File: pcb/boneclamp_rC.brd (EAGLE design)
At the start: 160 x 100 mm, 129 parts, among them IC1 24C, U1 AD8032ARZ-REEL7, U10 ADA4841-2YRZ, U11 ADA4841-2YRZ, U2 LT1964ES5-5TRMPBF, U3 ADA4841-2YRZ, U4 TLV70245DBVT, U5 ADA4841-2YRZ, U6 AD713JRZ-16, U7 AD7682BCPZ, U8 TPS63700DRCT, U9 ADA4841-2YRZ

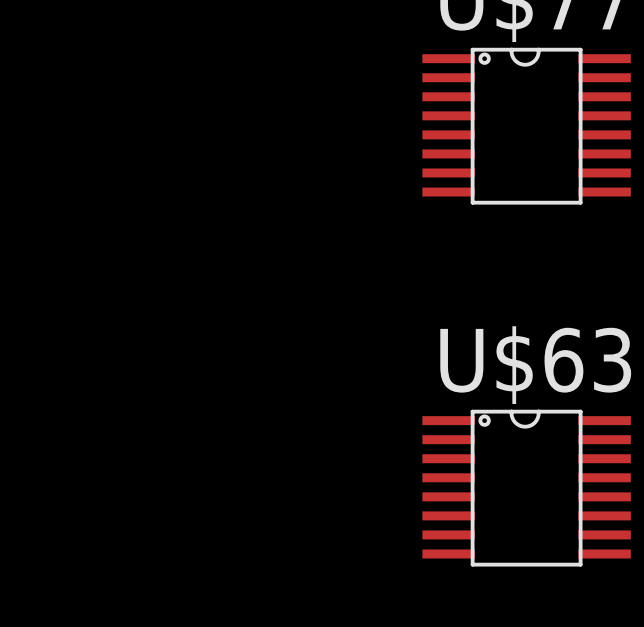
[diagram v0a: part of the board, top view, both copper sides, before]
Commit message: Added the 8331 to schematic. I'm pretty sure this is the right ADC.
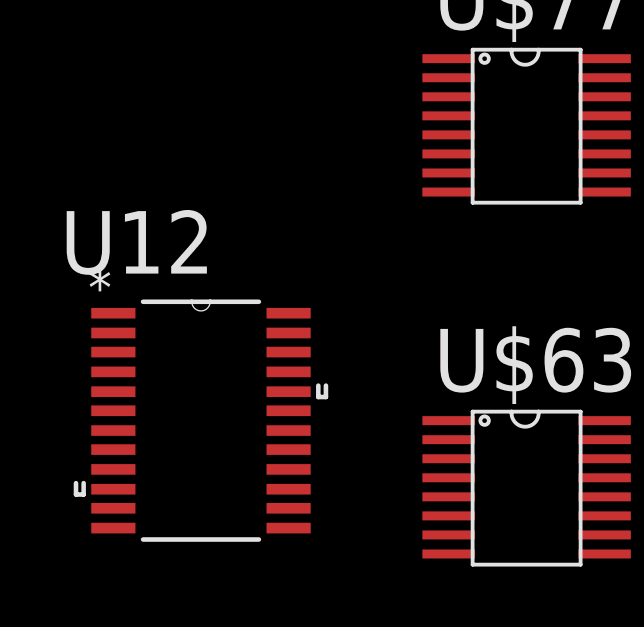
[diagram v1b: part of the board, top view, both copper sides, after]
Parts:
- added U12: ADS8331IBPW, ti-extended:SOP65P640X120-24N
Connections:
- new net VA: U12.17
- new net VBD: U12.16
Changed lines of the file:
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@@
 <element name="U$77" library="ti-extended" package="SOP63P500X150-16N" value="ADS8343" x="-120.015" y="-573.405"/>
 <element name="U$63" library="ti-extended" package="SOP63P500X150-16N" value="ADS8343" x="-120.015" y="-585.47"/>
+<element name="U12" library="ti-extended" package="SOP65P640X120-24N" value="ADS8331IBPW" x="-128.27" y="-585.47">
+<attribute name="PACKAGE" value="TSSOP-24" x="-128.27" y="-585.47" size="1.778" layer="27" display="off"/>
+<attribute name="OC_NEWARK" value="27T6163" x="-128.27" y="-585.47" size="1.778" layer="27" display="off"/>
+<attribute name="MPN" value="ADS8331IBPW" x="-128.27" y="-585.47" size="1.778" layer="27" display="off"/>
+<attribute name="SUPPLIER" value="Texas Instruments" x="-128.27" y="-585.47" size="1.778" layer="27" display="off"/>
+<attribute name="OC_FARNELL" value="1882255" x="-128.27" y="-585.47" size="1.778" layer="27" display="off"/>
+</element>
 </elements>
 <signals>
@@
 <wire x1="-120.015" y1="-573.405" x2="-114.815" y2="-577.85" width="0" layer="19" extent="1-1"/>
 </signal>
+<signal name="VA">
+<contactref element="U12" pad="17"/>
+</signal>
+<signal name="VBD">
+<contactref element="U12" pad="16"/>
+</signal>
 </signals>

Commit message: Minor fixes to voltage bias followers
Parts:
- removed C36, C37, C38, C39: (no value), resistor:C025-025X050
- removed R19: 6.937k, resistor:0204V
- removed R20: 10k, resistor:0204V
- removed R23, R24, R25, R26, R27, R28, R29, R30: (no value), resistor:0204V
- removed U3: ADA4841-2YRZ, analog-devices-01:SOIC127P600X175-8N
- added D2, D3, D4, D5: 1N4004, diode:DO41-10
- added IC2, IC3: LM741D, linear:SO08
- added R34, R35, R45: 1k, resistor:0204V
- added R46: (no value), rcl:PT-10S
- C25, C28: value (none) -> 0.1uF; device resistor:C025-025X050 -> rcl:C0805
- R21: value 6.66k -> (none); device resistor:0204V -> rcl:PT-10S
- R22: value 10k -> 1k
- moved C28 204.4 mm to (-141.6, -645.8)
- moved C25 196.8 mm to (-141.6, -639.4)
- moved R22 189.2 mm to (-141.0, -633.1)
- moved R21 163.6 mm to (-138.4, -609.6)
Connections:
- removed net N$3: R26.2, R30.1, U6.14
- removed net N$52: R25.2, R29.1, U6.12
- removed net N$53: C38.2, R21.1, R22.2, U3.5
- removed net N$54: C28.2, R19.1, R20.2, U3.3
- removed net N$55: R24.2, R28.1, U6.5
- removed net N$56: R23.2, R27.1, U6.3
- removed net N$57: C25.2, R20.1
- removed net N$58: C37.1
- removed net N$59: R22.1
- new net .5VREF-: IC2.2, R21.1, R34.1, R35.2
- new net .5VREF-1: C25.1, IC3.2, R46.1
- new net N$10: IC3.3, R22.1, R45.2
- new net N$12: C28.1, R35.1
- net GND: now also C28.2, IC2.3, R45.1; no longer C25.1, C28.1, C36.1, C38.1, C39.1
- net VBIAS_DOWN: now also D2.C, D3.C, D4.C, D5.C, IC2.6, R21.2; no longer C39.2, U3.6, U3.7
- net VBIAS_UP: now also IC3.6, R46.2; no longer C36.2, U3.1, U3.2
- net VDD: now also IC2.7, IC3.7; no longer R19.2, U3.8
- net VREF: now also R22.2, R34.2
- net VSS: now also IC2.4, IC3.4; no longer R21.2, U3.4
- net _DAC_A: now also D2.A, U6.14; no longer R23.1, R30.2
- net _DAC_B: now also D5.A, U6.3; no longer R26.1, R27.2
- net _DAC_C: now also D4.A, U6.5; no longer R25.1, R28.2
- net _DAC_D: now also D3.A, U6.12; no longer R24.1, R29.2

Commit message: Finished basics of input stage to new 8331 and some of the digital interface for it.
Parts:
- removed C11: 10uF, rcl:C0805
- removed C12, C13, C14: 0.1uF, rcl:C0805
- removed SJ6, SJ7, SJ8: (no value), jumper:SJ
- removed U$77: ADS8343, ti-extended:SOP63P500X150-16N
- removed U7: AD7682BCPZ, analog-devices-02:QFN50P400X400X100-21N
- added C36, C37: 0.1uF, rcl:C0603
- added C39, C47: 1uF, rcl:C0603
- added C48: (no value), rcl:C0805
- added C55, C56: 4.7uF, rcl:C0603
- added C57, C58, C59, C64, C65, C66, C67, C68, C69: 0.1uF, rcl:C0805
- added C60, C61, C62, C63: 1nF, rcl:C0603
- added R19, R20, R29, R30, R47, R48, R49, R50: 10k, rcl:R0603
- added R23: 10k,1%, resistor:R0805
- added R24: 1k, resistor:R0805
- added R25, R26, R27, R28: 20, rcl:R0603
- added R51: 20k,1%, resistor:R0805
- added SJ5, SJ9: (no value), jumper:SJ
- added TP8, TP9: TPB1,27, testpad:B1,27
- added U13, U15, U16, U3: OPA365AIDBVR, ti-extended:SOT95P280X145-5N
- added U14: REF5040MDREP, ti-extended:SOIC127P600X175-8N
- U$63: value ADS8343 -> OPA735BVT; device ti-extended:SOP63P500X150-16N -> ti-extended:SOT23-5L
- moved R14 692.0 mm to (-141.6, -956.3)
- moved C10 690.7 mm to (-123.2, -943.6)
- moved U1 630.0 mm to (-139.7, -934.1)
- moved R15 629.1 mm to (-135.9, -950.0)
- moved C1 628.9 mm to (-128.9, -943.6)
- moved R16 622.5 mm to (-127.6, -950.0)
- moved C3 613.8 mm to (-141.6, -979.8)
- moved C2 588.4 mm to (-141.6, -943.6)
- moved C46 432.1 mm to (-135.3, -943.6)
- moved U$63 140.7 mm to (-141.6, -724.5)
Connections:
- removed net ADC_SCLK: U7.13
- removed net ADC_SDI: SJ7.1
- removed net ADC_SDID: SJ8.1
- removed net N$11: SJ7.2, SJ8.2, U7.12
- removed net N$28: C11.1, R14.2, U7.2
- removed net N$34: C14.1, U7.3
- removed net VA: U12.17
- removed net VBD: U12.16
- removed net VCC: U$63.1, U$63.9, U$77.1, U$77.9
- removed net VCOM: U7.10
- new net ADC_CDI: SJ9.1
- new net ADC_CS: U12.11
- new net AGND1: C57.2, U12.14
- new net N$13: R47.1, R48.2, U15.4
- new net N$15: R49.1, R50.2, U16.4
- new net N$24: U12.21, U12.22
- new net N$26: R23.1, R51.2, U$63.4
- new net N$3: R19.1, R20.2, U3.4
- new net N$32: C47.2, U14.5
- new net N$35: SJ5.2, U12.13
- new net N$36: SJ9.2, U12.9
- new net N$37: C55.1, C56.1, C60.1, C61.1, C62.1, C63.1, U12.19, U12.20
- new net N$40: C60.2, R25.1, U12.24
- new net N$41: C61.2, R26.1, U12.1
- new net N$42: C62.2, R27.1, U12.2
- new net N$43: C63.2, R28.1, U12.3
- new net N$6: R29.1, R30.2, U13.4
- new net VBIAS+: U13.3, U15.3, U16.3, U3.3
- new net VBIAS-: C3.1, R23.2, R24.1, TP8.TP
- new net _VREF: C48.1, R14.2, R51.1, TP9.TP, U14.6
- net ADC_A: now also R19.2
- net ADC_B: now also R29.2
- net ADC_C: now also R47.2
- net ADC_CNV: now also U12.15; no longer U7.11
- net ADC_D: now also R49.2
- net ADC_SDO: now also SJ5.1; no longer SJ6.2
- net AGND: now also C36.1, C37.1, C39.1, C47.1, C48.2, C58.2, C59.2, C64.2, C65.2, C66.2, C67.2, C68.2, C69.2, U$63.3, U14.4; no longer C11.2, C12.2, C13.2, C14.2, U$42.10, U7.21, U7.4, U7.5
- net GND: no longer U$63.10, U$63.11, U$77.10, U$77.11
- net N$9: now also R24.2, U$63.1; no longer SJ6.1
- net VDD: now also C37.2, C39.2, C55.2, C59.1, C65.1, C67.1, C69.1, U$63.5, U12.17, U13.5, U14.2, U15.5, U16.5, U3.5; no longer C13.1, C3.1, U7.1, U7.20
- net VDRIVE: now also C57.1, U$42.10, U12.16; no longer C12.1, U7.15
- net VREF: now also C56.2, U12.18
- net VSS: now also C36.2, C58.1, C64.1, C66.1, C68.1, U$63.2, U13.2, U15.2, U16.2, U3.2
- net _ADC_A: now also R20.1, R25.2, U3.1; no longer U7.16
- net _ADC_B: now also R26.2, R30.1, U13.1; no longer U7.18
- net _ADC_C: now also R27.2, R48.1, U15.1; no longer U7.7
- net _ADC_D: now also R28.2, R50.1, U16.1; no longer U7.9

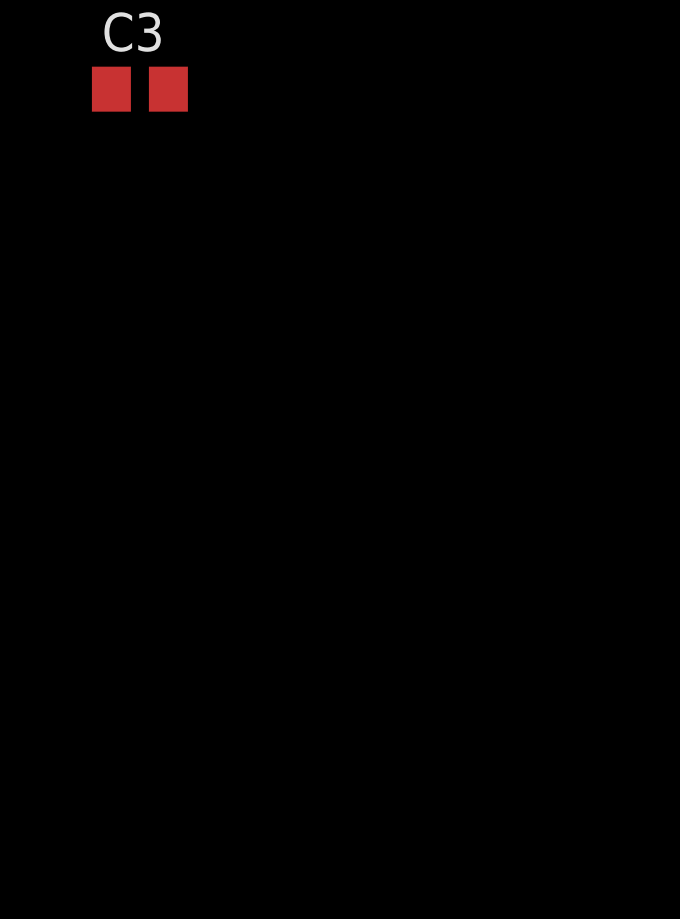
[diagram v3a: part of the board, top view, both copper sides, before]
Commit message: Added the switched capacitor voltage inveter, which greatly simiplifies the power supply design.
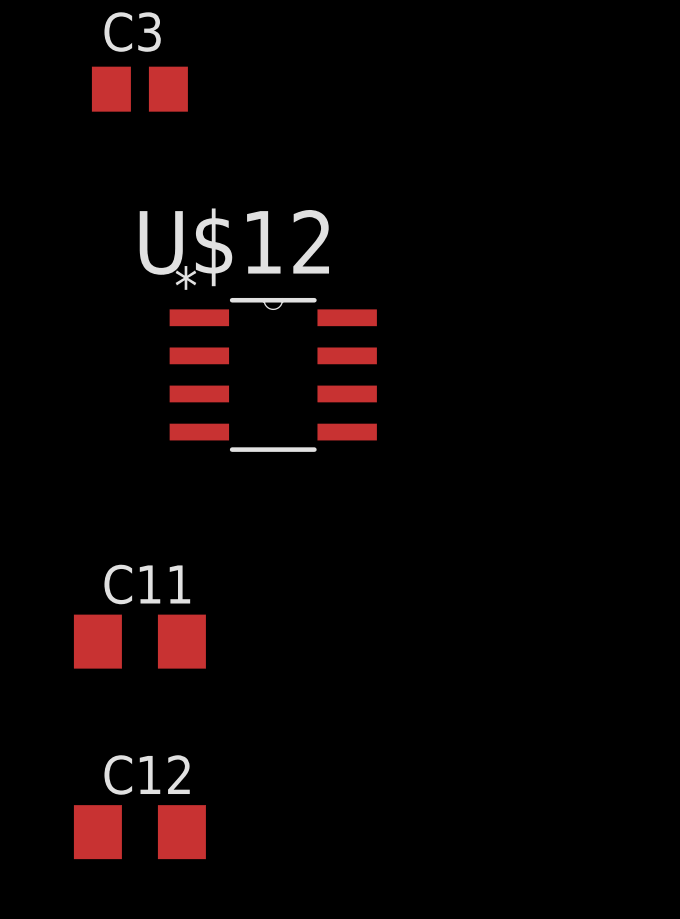
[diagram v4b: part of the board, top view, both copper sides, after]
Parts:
- added C11, C12: 47uF, rcl:C1206
- added U$12: LM2663, ti-extended:SOIC127P600X175-8N
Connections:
- new net N$33: C12.1, U$12.2
- new net N$34: C12.2, U$12.4
- new net SD: U$12.1
- net AGND: now also C11.1, U$12.3, U$12.6
- net VDD_5V: now also U$12.8
- net _VSS: now also C11.2, U$12.5
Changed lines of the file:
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@@
 <element name="R24" library="resistor" package="R0805" value="1k" x="-141.605" y="-973.455"/>
 <element name="C3" library="rcl" package="C0805" value="10uF" x="-141.605" y="-979.805"/>
+<element name="U$12" library="ti-extended" package="SOIC127P600X175-8N" value="LM2663" x="-137.16" y="-989.33"/>
+<element name="C11" library="rcl" package="C1206" value="47uF" x="-141.605" y="-998.22"/>
+<element name="C12" library="rcl" package="C1206" value="47uF" x="-141.605" y="-1004.57"/>
 </elements>
 <signals>
@@
 <contactref element="C46" pad="2"/>
 <contactref element="C3" pad="2"/>
+<contactref element="U$12" pad="6"/>
+<contactref element="U$12" pad="3"/>
+<contactref element="C11" pad="1"/>
 <wire x1="-134.305" y1="-873.76" x2="-140.655" y2="-873.76" width="0" layer="19" extent="1-1"/>
 <wire x1="-140.655" y1="-895.985" x2="-140.655" y2="-873.76" width="0" layer="19" extent="1-1"/>
@@
 <wire x1="-126.785" y1="-949.96" x2="-127.955" y2="-943.61" width="0" layer="19" extent="1-1"/>
 <wire x1="-140.655" y1="-979.805" x2="-126.785" y2="-949.96" width="0" layer="19" extent="1-1"/>
+<wire x1="-139.6238" y1="-989.965" x2="-140.655" y2="-979.805" width="0" layer="19" extent="1-1"/>
+<wire x1="-134.6962" y1="-989.965" x2="-139.6238" y2="-989.965" width="0" layer="19" extent="1-1"/>
+<wire x1="-143.005" y1="-998.22" x2="-139.6238" y2="-989.965" width="0" layer="19" extent="1-1"/>
 <wire x1="-140.655" y1="-815.975" x2="-140.655" y2="-873.76" width="0" layer="19" extent="1-1"/>
 <wire x1="-140.655" y1="-809.625" x2="-140.655" y2="-815.975" width="0" layer="19" extent="1-1"/>
@@
 <contactref element="C8" pad="1"/>
 <contactref element="U4" pad="3"/>
+<contactref element="U$12" pad="8"/>
 <wire x1="-62.4332" y1="-74.6506" x2="-69.43" y2="-76.2" width="0" layer="19" extent="1-1"/>
 <wire x1="-61.81" y1="-76.2" x2="-62.4332" y2="-74.6506" width="0" layer="19" extent="1-1"/>
@@
 <wire x1="50.165" y1="24.13" x2="-60.96" y2="-69.43" width="0" layer="19" extent="1-1"/>
 <wire x1="52.705" y1="24.13" x2="50.165" y2="24.13" width="0" layer="19" extent="1-1"/>
+<wire x1="-134.6962" y1="-987.425" x2="-84.67" y2="-229.87" width="0" layer="19" extent="1-1"/>
 </signal>
 <signal name="N$17">
@@
 <contactref element="C5" pad="1"/>
 <contactref element="U2" pad="4"/>
+<contactref element="U$12" pad="5"/>
+<contactref element="C11" pad="2"/>
 <wire x1="-81.3308" y1="-169.8498" x2="-83.7692" y2="-168.91" width="0" layer="19" extent="1-1"/>
 <wire x1="-84.67" y1="-177.8" x2="-81.3308" y2="-169.8498" width="0" layer="19" extent="1-1"/>
@@
 <wire x1="-59.4868" y1="-73.66" x2="-84.67" y2="-109.22" width="0" layer="19" extent="1-1"/>
 <wire x1="-54.25" y1="-74.93" x2="-59.4868" y2="-73.66" width="0" layer="19" extent="1-1"/>
+<wire x1="-134.6962" y1="-991.235" x2="-84.67" y2="-177.8" width="0" layer="19" extent="1-1"/>
+<wire x1="-140.205" y1="-998.22" x2="-134.6962" y2="-991.235" width="0" layer="19" extent="1-1"/>
 </signal>
 <signal name="N$27">
@@
 <wire x1="-140.755" y1="-973.455" x2="-142.555" y2="-725.835" width="0" layer="19" extent="1-1"/>
 </signal>
+<signal name="SD">
+<contactref element="U$12" pad="1"/>
+</signal>
+<signal name="N$34">
+<contactref element="U$12" pad="4"/>
+<contactref element="C12" pad="2"/>
+<wire x1="-139.6238" y1="-991.235" x2="-140.205" y2="-1004.57" width="0" layer="19" extent="1-1"/>
+</signal>
+<signal name="N$33">
+<contactref element="C12" pad="1"/>
+<contactref element="U$12" pad="2"/>
+<wire x1="-139.6238" y1="-988.695" x2="-143.005" y2="-1004.57" width="0" layer="19" extent="1-1"/>
+</signal>
 </signals>

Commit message: Minor changes.
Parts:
- removed C23: 10uF, rcl:C0603
- removed C24: 22nF, rcl:C0603
- removed C26: 0.1uF, rcl:C0603
- removed C27: 4.7nF, rcl:C0603
- removed C29: 10nF, rcl:C0603
- removed C30, C31, C32, C33: 4.7uF, rcl:C0603
- removed C34: 0.22uF, rcl:C0603
- removed C35: 10pF, rcl:C0603
- removed D1: (no value), boneclamp:DO-219AB
- removed L1: 4.7uH, boneclamp:L4012M
- removed R12: 750, rcl:R0603
- removed R13: 150k, rcl:R0603
- removed R5: 100k, rcl:R0603
- removed U8: TPS63700DRCT, ti-extended:SON50P300X300X100-11N
- moved C3 1011.5 mm to (229.2, -38.7)
- moved C58 1011.5 mm to (229.2, 131.4)
- moved C60 1011.5 mm to (228.6, 99.1)
- moved C62 1011.5 mm to (228.6, 88.9)
- moved C63 1011.5 mm to (228.6, 83.8)
- moved C64 1011.5 mm to (229.2, 67.3)
- moved C65 1011.5 mm to (235.6, 67.3)
- moved R14 1011.5 mm to (229.2, -15.2)
- moved R26 1011.5 mm to (228.6, 114.3)
- moved R28 1011.5 mm to (228.6, 104.1)
- moved R29 1011.5 mm to (241.3, 67.9)
- moved R50 1011.5 mm to (228.6, 17.1)
- moved R51 1011.5 mm to (229.2, -21.0)
- moved C1 1011.5 mm to (241.9, -2.54)
- moved C10 1011.5 mm to (247.7, -2.54)
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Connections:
- removed net N$23: C26.1, R5.2, U8.3, U8.4
- removed net N$25: C27.1, U8.1
- removed net N$27: D1.P$1, L1.1, U8.6
- removed net N$30: C35.1, R12.2, R13.1, U8.9
- removed net N$31: C34.1, R13.2, U8.10
- net AGND: no longer C23.2, C24.2, C26.2, C27.2, C29.2, C30.2, C31.2, C32.2, C33.2, C34.2, L1.2, U8.11, U8.2, U8.7
- net VDD_5V: no longer C23.1, C24.1, R5.1, U8.5
- net _VSS: no longer C29.1, C30.1, C31.1, C32.1, C33.1, C35.2, D1.P$2, R12.1, U8.8

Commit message: Minor changes.
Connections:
- removed net VBIAS: C46.1, U1.6, U1.7
- net VBIAS+: now also C46.1, U1.6, U1.7
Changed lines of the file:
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@@
 <wire x1="233.6038" y1="5.08" x2="240.985" y2="-2.54" width="0" layer="19" extent="1-1"/>
-</signal>
-<signal name="VBIAS">
-<contactref element="U1" pad="6"/>
-<contactref element="U1" pad="7"/>
-<contactref element="C46" pad="1"/>
-<wire x1="233.6038" y1="6.35" x2="234.635" y2="-2.54" width="0" layer="19" extent="1-1"/>
-<wire x1="233.6038" y1="7.62" x2="233.6038" y2="6.35" width="0" layer="19" extent="1-1"/>
 </signal>
 <signal name="_VREF">
@@
 <contactref element="U15" pad="3"/>
 <contactref element="U16" pad="3"/>
-<wire x1="229.8446" y1="52.4002" x2="229.8446" y2="74.6252" width="0" layer="19" extent="1-1"/>
-<wire x1="229.8446" y1="30.1752" x2="229.8446" y2="52.4002" width="0" layer="19" extent="1-1"/>
-<wire x1="-140.9954" y1="-683.5648" x2="229.8446" y2="74.6252" width="0" layer="19" extent="1-1"/>
+<contactref element="U1" pad="6"/>
+<contactref element="U1" pad="7"/>
+<contactref element="C46" pad="1"/>
+<wire x1="233.6038" y1="6.35" x2="233.6038" y2="7.62" width="0" layer="19" extent="1-1"/>
+<wire x1="234.635" y1="-2.54" x2="233.6038" y2="6.35" width="0" layer="19" extent="1-1"/>
+<wire x1="229.8446" y1="30.1752" x2="233.6038" y2="7.62" width="0" layer="19" extent="1-1"/>
+<wire x1="229.8446" y1="52.4002" x2="229.8446" y2="30.1752" width="0" layer="19" extent="1-1"/>
+<wire x1="229.8446" y1="74.6252" x2="229.8446" y2="52.4002" width="0" layer="19" extent="1-1"/>
+<wire x1="-140.9954" y1="-683.5648" x2="234.635" y2="-2.54" width="0" layer="19" extent="1-1"/>
 </signal>
 <signal name="N$9">
